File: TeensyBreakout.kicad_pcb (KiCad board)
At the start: 2 copper layers, 114 x 115.1 mm, 112 parts, among them CON2 Headphone, CON3 Line In, IC1 ZLDO1117G33, IC2 NCP1117ST50T3G, J1 73725-0110BLF, J2 Conn_01x04, J3 RJ45_LED, J4 PJ-102A, J5 OSTTC022162 (R), J6 OSTTC022162 (L), Q1 FDN340P, Q1A1 BSD223P, Q1B1 BSD223P, Q6 BC107, SW1 SW_MEC_5E, U1 Teensy4.1, U5 SGTL5000XNAA3, U6 TDA7265

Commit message: svgs exported
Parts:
- moved JP13 121.5 mm to (30.1, 48.5), turned to 0 degrees
- moved SJ4 67.8 mm to (119.1, 121.6)
- moved JP22 25.7 mm to (35.3, 61.2), turned to 270 degrees
- moved C39 17.0 mm to (45.0, 118.3), turned to 90 degrees
- moved C38 15.1 mm to (46.5, 118.3), turned to 90 degrees
- moved JP12 9.87 mm to (28.6, 59.4)
- moved C3 1.96 mm to (44.4, 103.0), turned to 90 degrees
- moved BT1 1.11 mm to (83.3, 102.9)
- moved C25 0.25 mm to (39.1, 46.6)
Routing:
- net Net-(C35-Pad2): track 0.00 -> 136.3 mm, vias 0 -> 2
- net Net-(C36-Pad2): track 0.00 -> 129.1 mm, vias 0 -> 2
- net /D0-RX1-CS1-CRX2: track 0.00 -> 95.4 mm, vias 0 -> 2
- net /D1-TX1-MISO1-CTX2: track 1.27 -> 88.1 mm, vias 0 -> 2
- net /D2-OUT2: track 0.00 -> 81.5 mm, vias 0 -> 2
- net /AmpV2/LINEIN_L: track 0.00 -> 78.8 mm, vias 0 -> 4
- net /AmpV2/LINEIN_R: track 0.00 -> 76.3 mm, vias 0 -> 4
- net /D3-LRCLK2: track 0.00 -> 75.7 mm, vias 0 -> 2
- net /D4-BCLK2: track 0.00 -> 68.2 mm, vias 0 -> 2
- net /D36-CS-PWM: track 0.00 -> 63.2 mm, vias 0 -> 3
- net /D37-CS-PWM: track 0.00 -> 62.9 mm, vias 0 -> 3
- net /D5-IN2: track 0.00 -> 62.8 mm, vias 0 -> 2
- net /D6-OUT1D: track 0.00 -> 58.8 mm, vias 0 -> 2
- net /D35-TX8: track 0.00 -> 57.7 mm, vias 0 -> 3
- net /D34-TX8: track 4.65 -> 58.3 mm, vias 0 -> 3
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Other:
- board size 114 x 115.1 mm -> 116.5 x 115.1 mm

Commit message: redoing traces
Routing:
- net /D38-A14-CS1-IN1: track 0.00 -> 104.3 mm, vias 0 -> 3
- net /ON-OFF: track 0.00 -> 101.5 mm, vias 0 -> 3
- net /D22-A8-CTX1: track 0.00 -> 95.4 mm, vias 0 -> 2
- net /D14-A0-TX3-SPDIF_OUT: track 0.00 -> 74.2 mm, vias 0 -> 1
- net /ESP-RST: track 12.7 -> 84.5 mm, vias 0 -> 2
- net /PGM: track 0.00 -> 68.8 mm, vias 0 -> 2
- net /ESP-PROG: track 3.58 -> 66.2 mm, vias 0 -> 4
- net /TEENSY_3V3: track 0.00 -> 54.5 mm, vias 0 -> 2
- net /VBAT: track 0.00 -> 47.2 mm, vias 0 -> 2
- net /D28-RX7: track 50.7 -> 96.0 mm
- net /D29-TX7: track 47.1 -> 90.5 mm
- net /D2-OUT2: track 81.5 -> 122.1 mm, vias 2 -> 5
- net /D23-A9-CRX1-MCLK1: track 0.00 -> 37.1 mm
- net /D0-RX1-CS1-CRX2: track 95.4 -> 129.8 mm
- net /D1-TX1-MISO1-CTX2: track 88.1 -> 120.1 mm, vias 2 -> 3
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
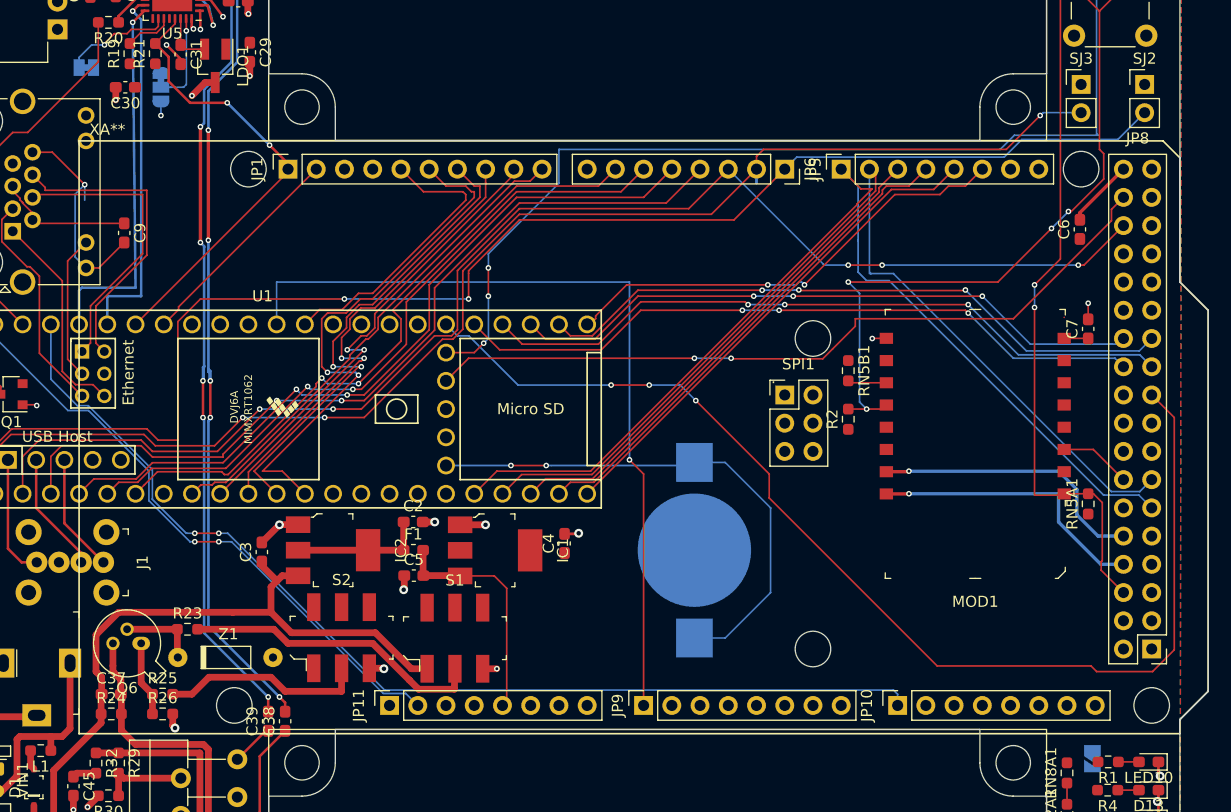
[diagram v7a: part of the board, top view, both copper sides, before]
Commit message: the back ports are wrong, need to rotate
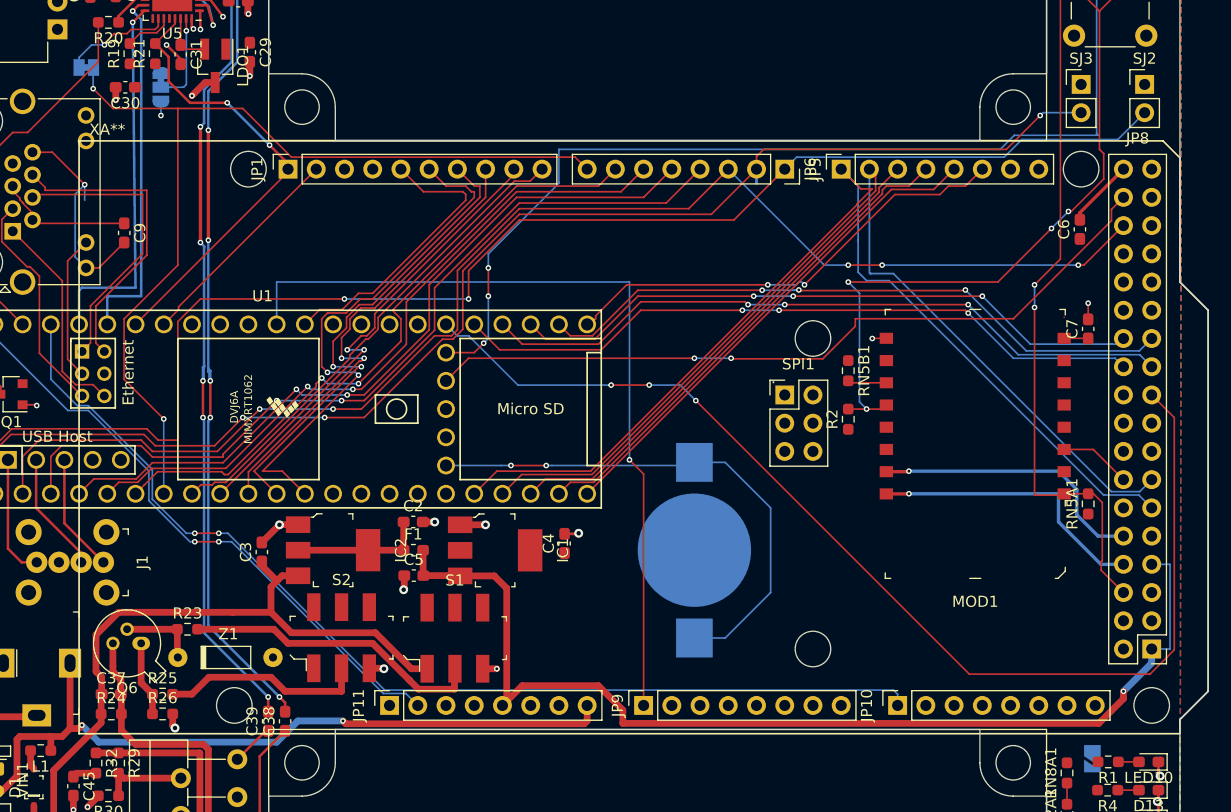
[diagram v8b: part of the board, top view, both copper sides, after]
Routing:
- net /D7-RX2-OUT1A: track 0.00 -> 87.5 mm, vias 0 -> 2
- net /5V_FUSE: track 21.0 -> 97.1 mm, vias 0 -> 1
- net /VIN+: track 18.2 -> 67.9 mm, vias 0 -> 2
- net /D38-A14-CS1-IN1: track 104.3 -> 103.3 mm
